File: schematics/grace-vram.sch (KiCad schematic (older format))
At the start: 15 parts, among them J10 GRACE board interface 1, J11 GRACE board interface 2, J12 15kHz Video Out, U10 VRAM

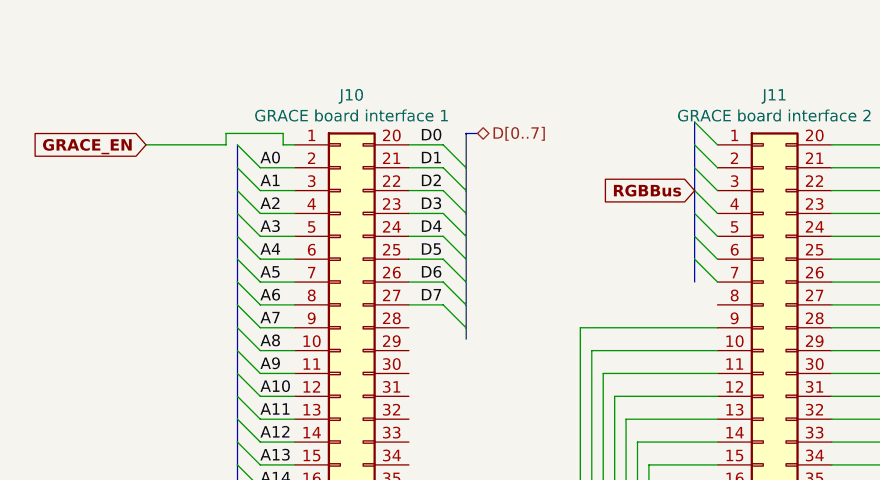
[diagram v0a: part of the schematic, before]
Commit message: add audio schematic, other fixes
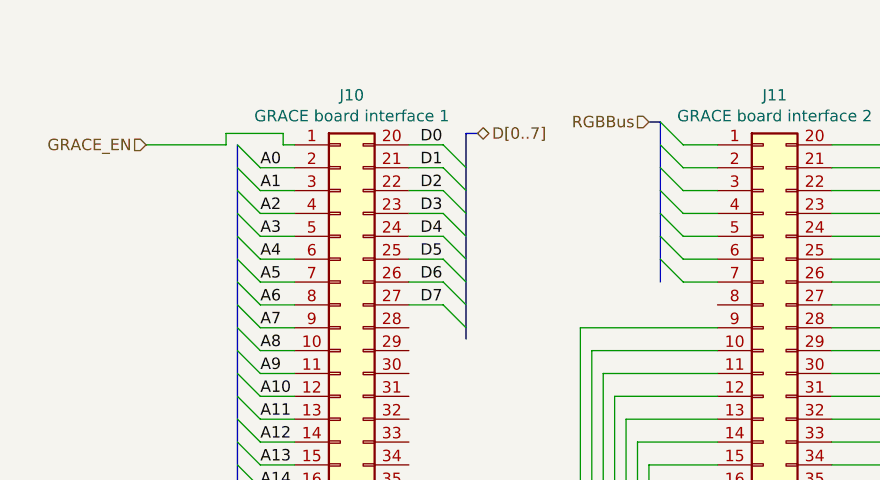
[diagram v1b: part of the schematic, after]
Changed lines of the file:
@@
 $Descr A4 11693 8268
 encoding utf-8
-Sheet 2 6
+Sheet 2 7
 Title ""
 Date ""
@@
 NoConn ~ 1750 2950
 NoConn ~ 2250 2950
-Text GLabel 1100 1150 0    50   Input ~ 10
-GRACE_EN
 Entry Wire Line
 	1500 1150 1600 1250
@@
 	2400 1850 2500 1950
 Entry Wire Line
-	3500 1050 3600 1150
-Entry Wire Line
-	3500 1150 3600 1250
-Entry Wire Line
-	3500 1250 3600 1350
-Entry Wire Line
-	3500 1350 3600 1450
-Entry Wire Line
-	3500 1450 3600 1550
-Entry Wire Line
-	3500 1550 3600 1650
-Entry Wire Line
-	3500 1650 3600 1750
-Text GLabel 3500 1350 0    50   Input ~ 10
-RGBBus
+	3350 1050 3450 1150
+Entry Wire Line
+	3350 1150 3450 1250
+Entry Wire Line
+	3350 1250 3450 1350
+Entry Wire Line
+	3350 1350 3450 1450
+Entry Wire Line
+	3350 1450 3450 1550
+Entry Wire Line
+	3350 1550 3450 1650
+Entry Wire Line
+	3350 1650 3450 1750
 $Comp
 L Connector:DB15_Female_HighDensity J12
@@
 Text Label 2300 1850 0    50   ~ 0
 D7
+Text HLabel 1100 1150 0    50   Input ~ 0
+GRACE_EN
+Wire Wire Line
+	3600 1150 3450 1150
+Wire Wire Line
+	3600 1250 3450 1250
+Wire Wire Line
+	3600 1350 3450 1350
+Wire Wire Line
+	3600 1450 3450 1450
+Wire Wire Line
+	3600 1550 3450 1550
+Wire Wire Line
+	3600 1650 3450 1650
+Wire Wire Line
+	3600 1750 3450 1750
 Wire Bus Line
-	3500 1050 3500 1750
+	3350 1050 3300 1050
+Wire Bus Line
+	3350 1050 3350 1750
 Wire Bus Line
 	8200 4000 9950 4000
@@
 Wire Bus Line
 	1500 1150 1500 2900
+Text HLabel 3300 1050 0    50   Input ~ 0
+RGBBus
 $EndSCHEMATC

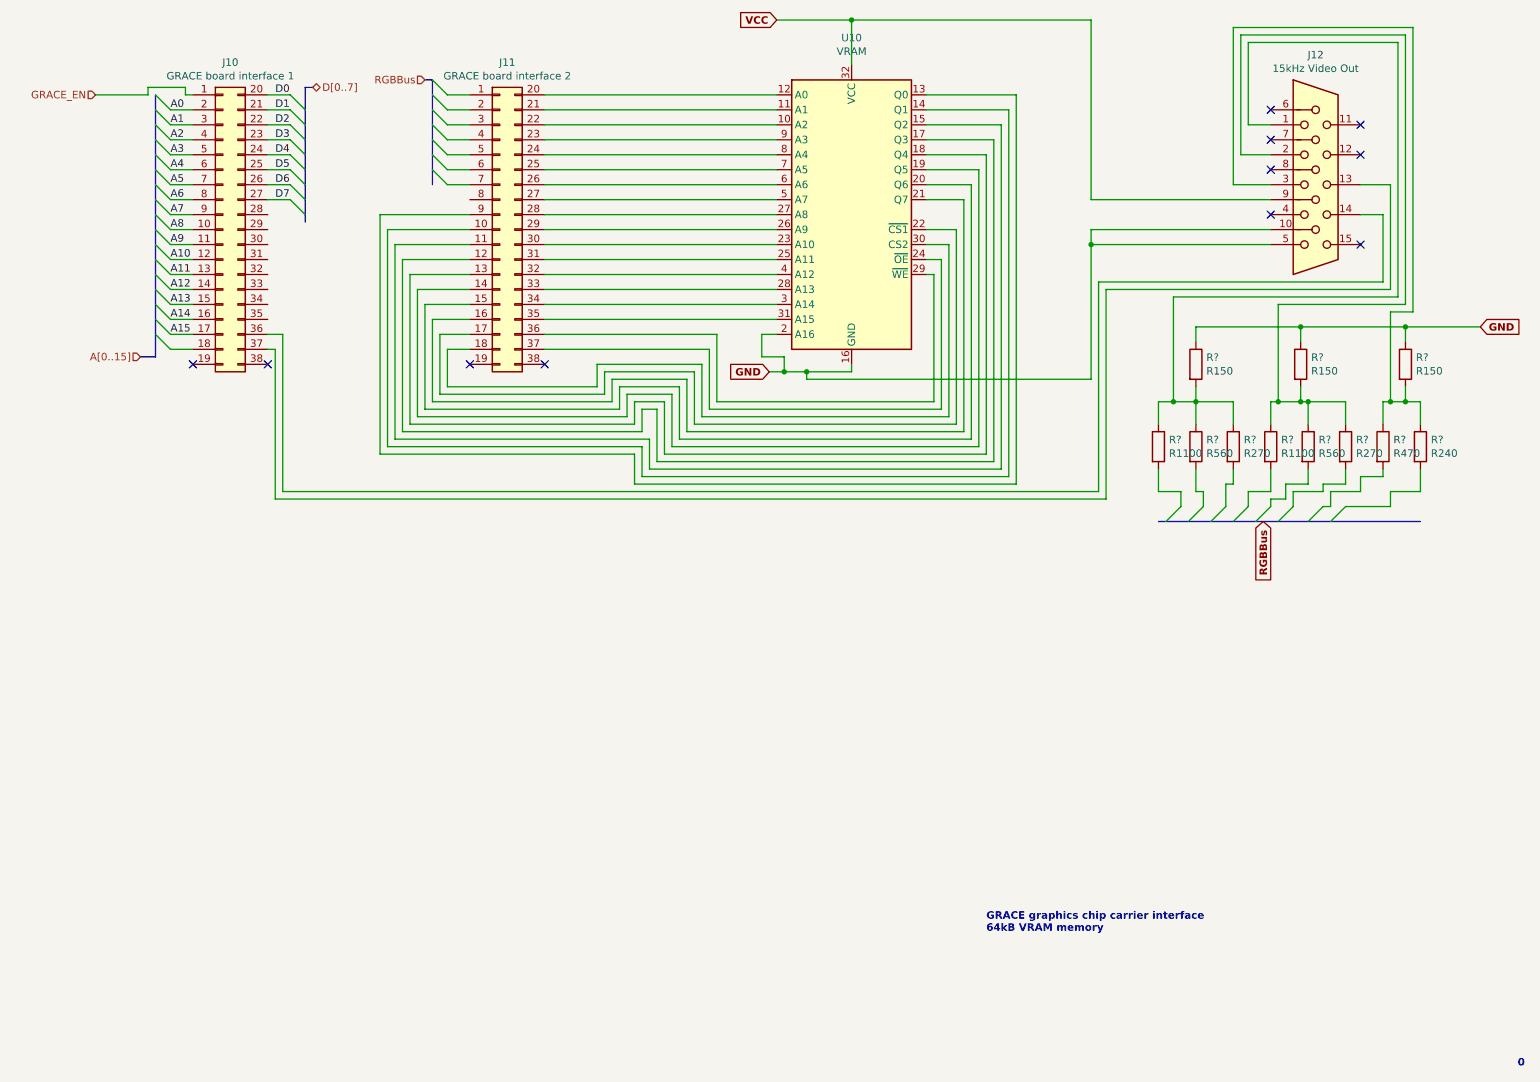
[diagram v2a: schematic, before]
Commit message: clean up, added nc pins
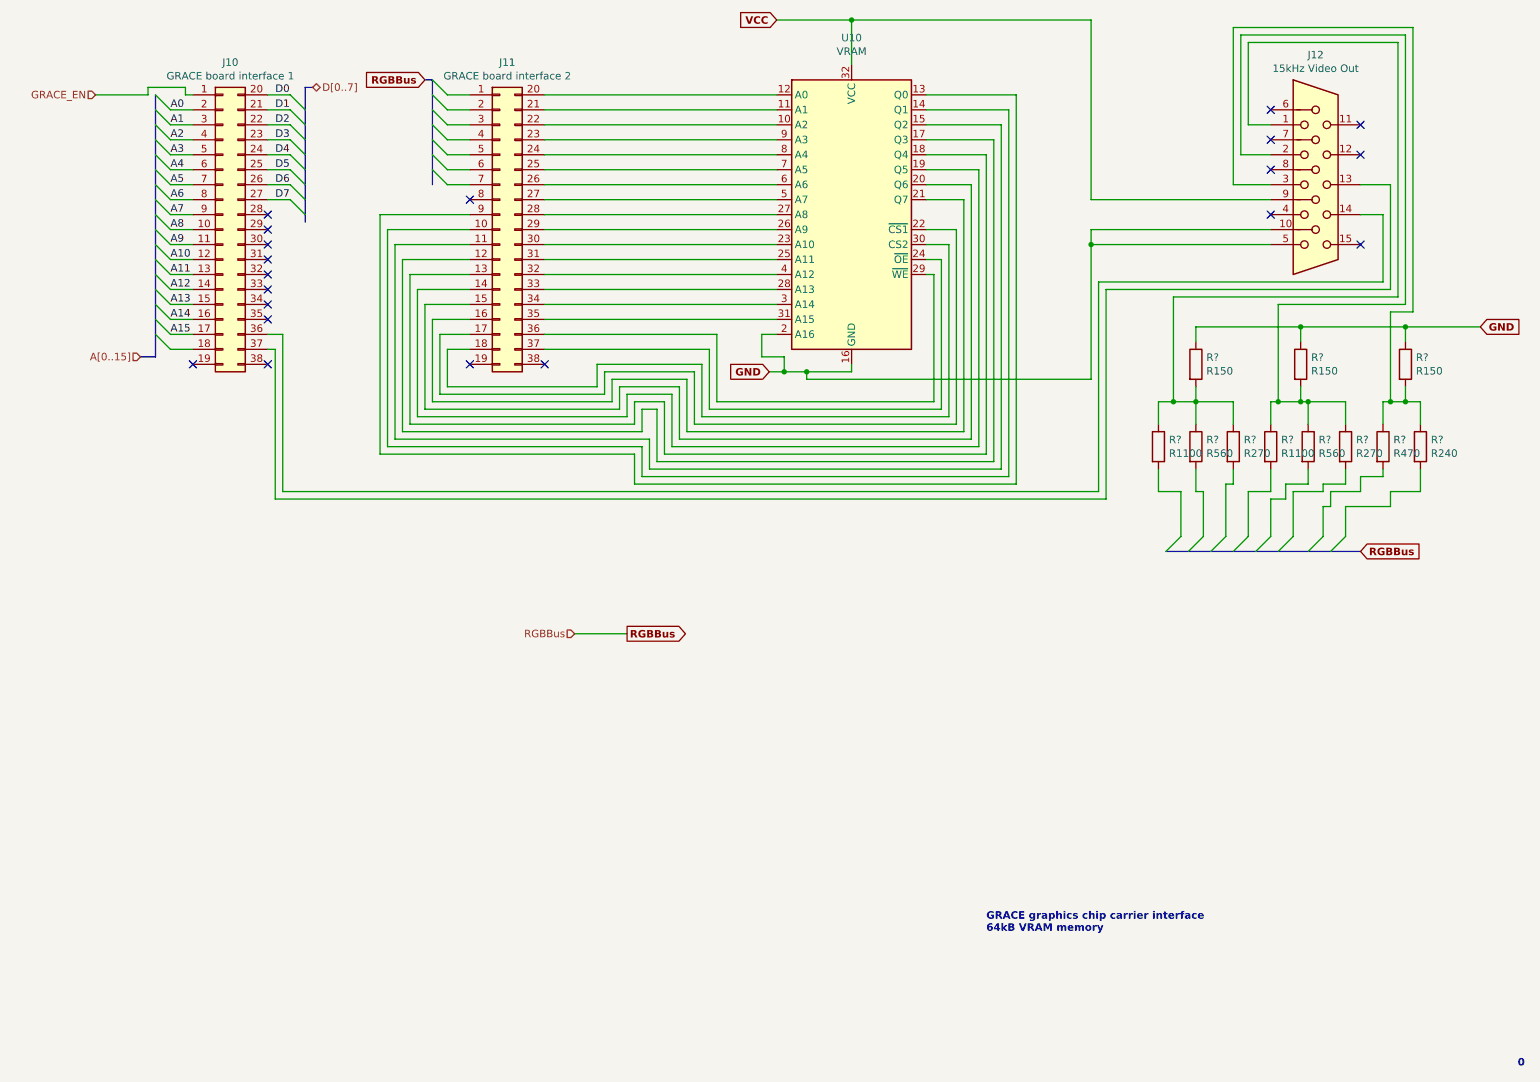
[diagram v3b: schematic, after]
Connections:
- no-connect marks 11 -> 20
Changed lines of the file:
@@
 	1    0    0    -1
 $EndComp
-Text GLabel 8900 4000 3    50   Input ~ 10
+Text GLabel 9550 4200 2    50   Input ~ 10
 RGBBus
 Entry Wire Line
-	8250 4000 8350 3900
-Entry Wire Line
-	8400 4000 8500 3900
-Entry Wire Line
-	8550 4000 8650 3900
-Entry Wire Line
-	8700 4000 8800 3900
-Entry Wire Line
-	8850 4000 8950 3900
-Entry Wire Line
-	9000 4000 9100 3900
-Entry Wire Line
-	9200 4000 9300 3900
-Entry Wire Line
-	9350 4000 9450 3900
-Wire Wire Line
-	8350 3900 8350 3800
+	8250 4200 8350 4100
+Entry Wire Line
+	8400 4200 8500 4100
+Entry Wire Line
+	8550 4200 8650 4100
+Entry Wire Line
+	8700 4200 8800 4100
+Entry Wire Line
+	8850 4200 8950 4100
+Entry Wire Line
+	9000 4200 9100 4100
+Entry Wire Line
+	9200 4200 9300 4100
+Entry Wire Line
+	9350 4200 9450 4100
 Wire Wire Line
 	8350 3800 8200 3800
@@
 	8200 3800 8200 3650
 Wire Wire Line
-	8500 3900 8500 3800
-Wire Wire Line
 	8500 3800 8450 3800
 Wire Wire Line
 	8450 3800 8450 3650
 Wire Wire Line
-	8650 3900 8650 3750
-Wire Wire Line
 	8650 3750 8700 3750
 Wire Wire Line
 	8700 3750 8700 3650
 Wire Wire Line
-	8800 3900 8800 3800
-Wire Wire Line
 	8800 3800 8950 3800
 Wire Wire Line
 	8950 3800 8950 3650
 Wire Wire Line
-	8950 3900 8950 3850
-Wire Wire Line
 	8950 3850 9050 3850
 Wire Wire Line
@@
 Wire Wire Line
 	9200 3750 9200 3650
-Wire Wire Line
-	9100 3900 9100 3800
 Wire Wire Line
 	9100 3800 9300 3800
@@
 Wire Bus Line
 	3350 1050 3300 1050
-Text HLabel 3300 1050 0    50   Input ~ 0
+Text HLabel 4300 4750 0    50   Input ~ 0
 RGBBus
+Wire Wire Line
+	8350 3800 8350 4100
+Wire Wire Line
+	8500 3800 8500 4100
+Wire Wire Line
+	8650 3750 8650 4100
+Wire Wire Line
+	8800 3800 8800 4100
+Wire Wire Line
+	8950 3850 8950 4100
+Wire Wire Line
+	9100 3800 9100 4100
+Wire Wire Line
+	9300 3900 9300 4100
+Wire Wire Line
+	9450 3900 9450 4100
+Text GLabel 4650 4750 2    50   Output ~ 10
+RGBBus
+Wire Wire Line
+	4300 4750 4650 4750
+Text GLabel 3300 1050 0    50   Input ~ 10
+RGBBus
+NoConn ~ 3600 1850
+NoConn ~ 2250 1950
+NoConn ~ 2250 2050
+NoConn ~ 2250 2150
+NoConn ~ 2250 2250
+NoConn ~ 2250 2350
+NoConn ~ 2250 2450
+NoConn ~ 2250 2550
+NoConn ~ 2250 2650
 Wire Bus Line
 	3350 1050 3350 1750
 Wire Bus Line
-	8200 4000 9950 4000
+	8250 4200 9550 4200
 Wire Bus Line
 	2500 1100 2500 2000

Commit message: Finish connecting hierarchial pins
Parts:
- added C?: C, symbol Device:C
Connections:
- wire segments 260 -> 262
- no-connect marks 20 -> 21
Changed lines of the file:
@@
 	1500 2650 1600 2750
-Entry Wire Line
-	1500 2750 1600 2850
 Entry Wire Line
 	2400 1150 2500 1250
@@
 	1600 2750 1750 2750
 Wire Wire Line
-	1600 2850 1750 2850
-Wire Wire Line
 	2250 1150 2400 1150
 Wire Wire Line
@@
 Wire Bus Line
 	3350 1050 3300 1050
-Text HLabel 4300 4750 0    50   Input ~ 0
-RGBBus
 Wire Wire Line
 	8350 3800 8350 4100
@@
 Wire Wire Line
 	9450 3900 9450 4100
-Text GLabel 4650 4750 2    50   Output ~ 10
-RGBBus
-Wire Wire Line
-	4300 4750 4650 4750
 Text GLabel 3300 1050 0    50   Input ~ 10
 RGBBus
-NoConn ~ 3600 1850
 NoConn ~ 2250 1950
 NoConn ~ 2250 2050
@@
 NoConn ~ 2250 2550
 NoConn ~ 2250 2650
+NoConn ~ 1750 2850
+NoConn ~ 3600 1850
+Text HLabel 4800 4850 0    50   Input ~ 0
+VCC
+Text HLabel 4800 5150 0    50   Input ~ 0
+GND
+$Comp
+L Device:C C?
+U 1 1 61DC964A
+P 5000 5000
+F 0 "C?" H 5115 5046 50  0000 L CNN
+F 1 "C" H 5115 4955 50  0000 L CNN
+F 2 "" H 5038 4850 50  0001 C CNN
+F 3 "~" H 5000 5000 50  0001 C CNN
+	1    5000 5000
+	1    0    0    -1
+$EndComp
+Text GLabel 5350 5150 2    50   Input ~ 10
+GND
+Text GLabel 5350 4850 2    50   Input ~ 10
+VCC
+Wire Wire Line
+	4800 4850 5000 4850
+Connection ~ 5000 4850
+Wire Wire Line
+	5000 4850 5350 4850
+Wire Wire Line
+	4800 5150 5000 5150
 Wire Bus Line
 	3350 1050 3350 1750
@@
 Wire Bus Line
 	1500 1150 1500 2900
+Connection ~ 5000 5150
+Wire Wire Line
+	5000 5150 5350 5150
 $EndSCHEMATC
